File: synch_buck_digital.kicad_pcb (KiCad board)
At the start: 4 copper layers, 60 x 49.6 mm, 48 parts, among them U1 BSC066N06NSATMA1, U2 BSC066N06NSATMA1, U3 INA241A3IDDFR

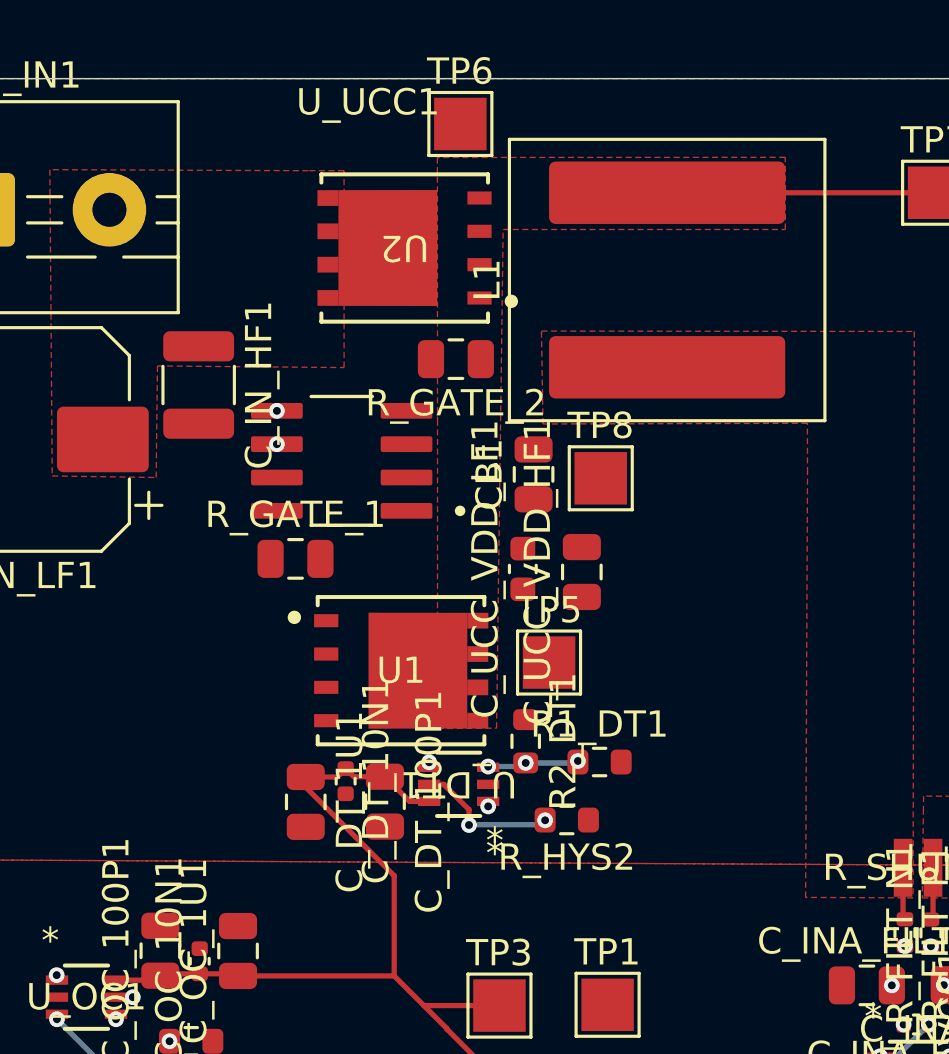
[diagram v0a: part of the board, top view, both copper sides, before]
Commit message: Fixed FET Footprint and updated pour topology
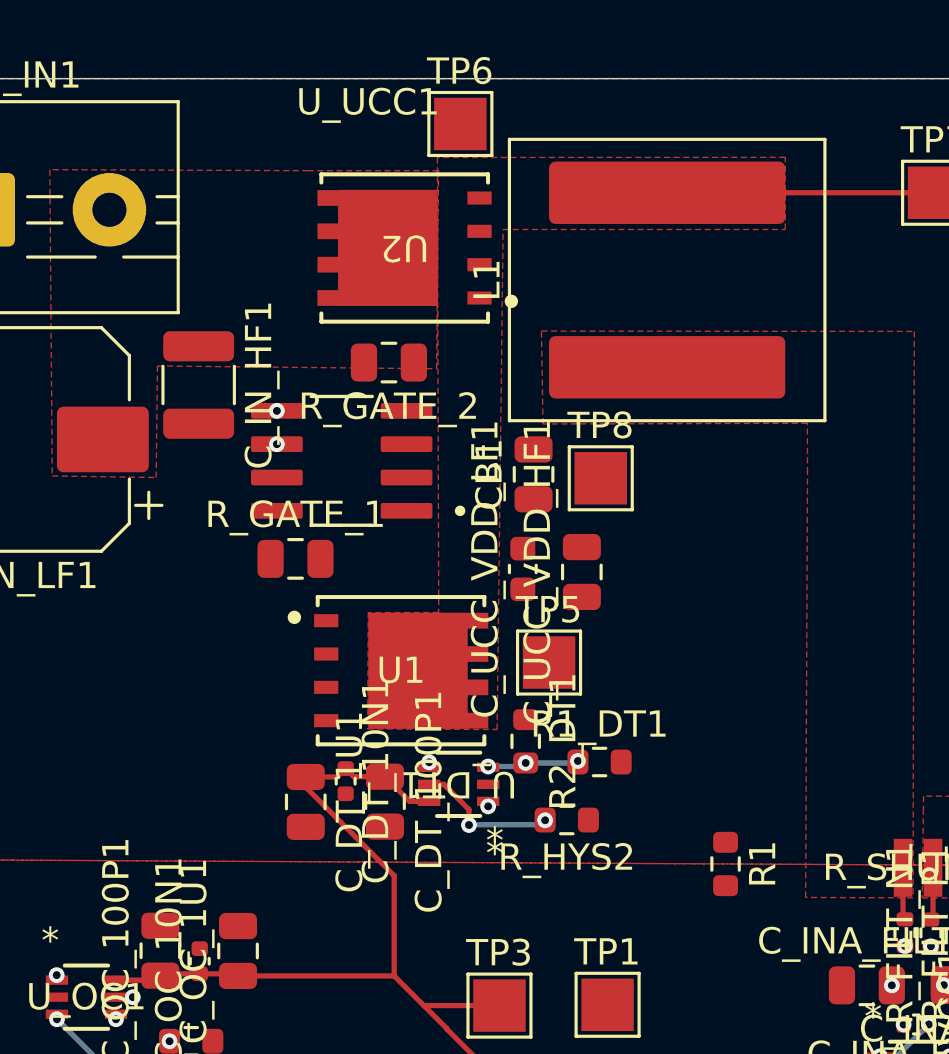
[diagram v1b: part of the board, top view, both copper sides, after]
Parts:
- added R1: 0R, Resistor_SMD:R_0603_1608Metric, F.Cu at (212.5, 83.9)
- moved R_GATE_2 2.55 mm to (199.7, 64.8)
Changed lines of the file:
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@@
 	(footprint "Capacitor_SMD:C_0805_2012Metric"
 		(layer "F.Cu")
-		(at 202.2 64.69 180)
+		(at 199.65 64.82 180)
 		(descr "Capacitor SMD 0805 (2012 Metric), square (rectangular) end terminal, IPC-7351 nominal, (Body size source: IPC-SM-782 page 76, https://www.pcb-3d.com/wordpress/wp-content/uploads/ipc-sm-782a_amendment_1_and_2.pdf, https://docs.google.com/spreadsheets/d/1BsfQQcO9C6DZCsRaXUlFlo91Tg2WpOkGARC1WS5S8t0/edit?usp=sharing)")
 		(tags "capacitor")
@@
 		)
 	)
+	(footprint "Resistor_SMD:R_0603_1608Metric"
+		(layer "F.Cu")
+		(at 212.475 83.925 -90)
+		(descr "Resistor SMD 0603 (1608 Metric), square (rectangular) end terminal, IPC-7351 nominal, (Body size source: IPC-SM-782 page 72, https://www.pcb-3d.com/wordpress/wp-content/uploads/ipc-sm-782a_amendment_1_and_2.pdf)")
+		(tags "resistor")
+		(property "Reference" "R1"
+			(at 0 -1.43 90)
+			(layer "F.SilkS")
+			(effects
+				(font
+					(size 1 1)
+					(thickness 0.15)
+				)
+			)
+		)
+		(property "Value" "0R"
+			(at 0 1.43 90)
+			(layer "F.Fab")
+			(effects
+				(font
+					(size 1 1)
+					(thickness 0.15)
+				)
+			)
+		)
+		(property "Datasheet" ""
+			(at 0 0 90)
+			(layer "F.Fab")
+			(hide yes)
+			(effects
+				(font
+					(size 1.27 1.27)
+				)
+			)
+		)
+		(property "Description" "Resistor, US symbol"
+			(at 0 0 90)
+			(layer "F.Fab")
+			(hide yes)
+			(effects
+				(font
+					(size 1.27 1.27)
+				)
+			)
+		)
+		(property "KiLib_Generator" "SMD_2terminal_chip_molded"
+			(at 0 0 90)
+			(layer "F.SilkS")
+			(hide yes)
+			(effects
+				(font
+					(size 1 1)
+					(thickness 0.15)
+				)
+			)
+		)
+		(property ki_fp_filters "R_*")
+		(sheetname "/")
+		(sheetfile "synch_buck_digital.kicad_sch")
+		(units
+			(unit
+				(name "A")
+				(pins "1" "2")
+			)
+		)
+		(attr smd)
+		(duplicate_pad_numbers_are_jumpers no)
+		(fp_line
+			(start -0.237258 0.5225)
+			(end 0.237258 0.5225)
+			(stroke
+				(width 0.12)
+				(type solid)
+			)
+			(layer "F.SilkS")
+		)
+		(fp_line
+			(start -0.237258 -0.5225)
+			(end 0.237258 -0.5225)
+			(stroke
+				(width 0.12)
+				(type solid)
+			)
+			(layer "F.SilkS")
+		)
+		(fp_rect
+			(start -1.48 -0.73)
+			(end 1.48 0.73)
+			(stroke
+				(width 0.05)
+				(type solid)
+			)
+			(fill no)
+			(layer "F.CrtYd")
+		)
+		(fp_rect
+			(start -0.8 -0.4125)
+			(end 0.8 0.4125)
+			(stroke
+				(width 0.1)
+				(type solid)
+			)
+			(fill no)
+			(layer "F.Fab")
+		)
+		(fp_text user "${REFERENCE}"
+			(at 0 0 90)
+			(layer "F.Fab")
+			(effects
+				(font
+					(size 0.4 0.4)
+					(thickness 0.06)
+				)
+			)
+		)
+		(pad "1" smd roundrect
+			(at -0.825 0 270)
+			(size 0.8 0.95)
+			(layers "F.Cu" "F.Mask" "F.Paste")
+			(roundrect_rratio 0.25)
+			(net "PGND")
+			(pintype "passive")
+		)
+		(pad "2" smd roundrect
+			(at 0.825 0 270)
+			(size 0.8 0.95)
+			(layers "F.Cu" "F.Mask" "F.Paste")
+			(roundrect_rratio 0.25)
+			(net "SGND")
+			(pintype "passive")
+		)
+		(embedded_fonts no)
+		(model "${KICAD10_3DMODEL_DIR}/Resistor_SMD.3dshapes/R_0603_1608Metric.step"
+			(offset
+				(xyz 0 0 0)
+			)
+			(scale
+				(xyz 1 1 1)
+			)
+			(rotate
+				(xyz 0 0 0)
+			)
+		)
+	)
 	(footprint "TestPoint:TestPoint_Pad_2.0x2.0mm"
 		(layer "F.Cu")
@@
 			(unit
 				(name "A")
-				(pins "1" "2" "3" "4" "8" "7" "6" "5")
+				(pins "1" "2" "3" "4" "9" "8" "7" "6" "5")
 			)
 		)
@@
 			)
 			(fill yes)
-			(layer "F.Cu")
-		)
-		(fp_poly
-			(pts
-				(xy 2.525501 -2.204999) (xy -1.240109 -2.2098) (xy -1.240109 2.2098) (xy 2.524502 2.204999) (xy 2.524502 1.605001)
-				(xy 2.524502 0.934999) (xy 2.524502 0.335001) (xy 2.524502 -0.335001) (xy 2.524502 -0.934999) (xy 2.525501 -1.605001)
-			)
-			(stroke
-				(width 0)
-				(type solid)
-			)
-			(fill yes)
 			(layer "F.Mask")
 		)
@@
 			(pintype "unspecified")
 		)
+		(pad "9" smd rect
+			(at -0.21 1.55 180)
+			(size 3.788772 4.425282)
+			(drill
+				(offset 0.856059 -1.546284)
+			)
+			(layers "F.Cu" "F.Mask" "F.Paste")
+			(net "+12V")
+			(pinfunction "EP_9")
+			(pintype "passive")
+		)
 		(embedded_fonts no)
 	)
@@
 			(unit
 				(name "A")
-				(pins "1" "2" "3" "4" "8" "7" "6" "5")
+				(pins "1" "2" "3" "4" "9" "8" "7" "6" "5")
 			)
 		)
@@
 			)
 			(fill yes)
-			(layer "F.Cu")
-		)
-		(fp_poly
-			(pts
-				(xy 2.525501 -2.204999) (xy -1.240109 -2.2098) (xy -1.240109 2.2098) (xy 2.524502 2.204999) (xy 2.524502 1.605001)
-				(xy 2.524502 0.934999) (xy 2.524502 0.335001) (xy 2.524502 -0.335001) (xy 2.524502 -0.934999) (xy 2.525501 -1.605001)
-			)
-			(stroke
-				(width 0)
-				(type solid)
-			)
-			(fill yes)
 			(layer "F.Mask")
 		)
@@
 			(pintype "unspecified")
 		)
+		(pad "9" smd rect
+			(at -0.21 1.55)
+			(size 3.788772 4.425282)
+			(drill
+				(offset 0.856059 -1.546284)
+			)
+			(layers "F.Cu" "F.Mask" "F.Paste")
+			(net "/SW")
+			(pinfunction "EP_9")
+			(pintype "passive")
+		)
 		(embedded_fonts no)
 	)
@@
 		(polygon
 			(pts
-				(xy 214.75 57) (xy 201.495599 57.005836) (xy 201.5 67) (xy 201.5 78.764999) (xy 203.75 78.75) (xy 204 59.75)
-				(xy 214.75 59.75)
+				(xy 214.75 57) (xy 201.495599 57.005836) (xy 201.545634 74.341902) (xy 198.86 74.35) (xy 198.842977 78.780458)
+				(xy 203.770542 78.799391) (xy 204 59.75) (xy 214.75 59.75)
 			)
 		)
@@
 		(polygon
 			(pts
-				(xy 186.73 57.47) (xy 186.82 69.14) (xy 190.78 69.2) (xy 190.83 64.95) (xy 197.94 65.01) (xy 197.94 57.51)
-				(xy 196.58 57.51)
+				(xy 186.73 57.47) (xy 186.82 69.14) (xy 190.78 69.2) (xy 190.83 64.95) (xy 201.464071 65.056988)
+				(xy 201.54 57.51) (xy 196.58 57.51)
 			)
 		)
@@
 		)
 		(min_thickness 0.25)
-		(fill yes
+		(fill
 			(thermal_gap 0.5)
 			(thermal_bridge_width 0.5)

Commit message: pcb finished
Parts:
- moved TP5 14.8 mm to (191.1, 78.3)
- moved C_UCC_VDD_HF1 10.3 mm to (196.7, 72.6), turned to 0 degrees
- moved R_GATE_2 8.72 mm to (202.1, 56.5)
- moved R_GATE_1 5.18 mm to (195.4, 77.4), turned to -90 degrees
- moved C_UCC_VDD_LF1 4.81 mm to (200.0, 72.1), turned to 180 degrees
- moved CB1 3.78 mm to (204.9, 72.8), turned to -90 degrees
- moved TP8 3.78 mm to (207.5, 73.0)
- moved TP6 3.72 mm to (206.0, 56.5)
- moved TP7 3.53 mm to (218.2, 61.0)
- moved L1 2.55 mm to (210.1, 64.2)
- moved C_INA_VCC1 0.61 mm to (222.7, 92.0)
- moved R1 0.16 mm to (212.5, 83.8)
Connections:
- C_DT_100P1 pad 2: SGND -> PGND
- C_DT_10N1 pad 2: SGND -> PGND
- C_DT_1U1 pad 2: SGND -> PGND
- U_UCC1 pad 7: SGND -> PGND
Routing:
- net Net-(U_UCC1-HO): track 0.00 -> 18.0 mm, vias 0 -> 2
- net +12V: track 0.00 -> 12.8 mm
- net /BOOT: track 0.00 -> 8.76 mm, vias 0 -> 3
- net /GATE_LS: track 0.00 -> 6.24 mm
- net Net-(U_UCC1-LO): track 0.00 -> 6.22 mm, vias 0 -> 2
- net /GATE_HS: track 0.00 -> 5.16 mm
- net SGND: track 0.00 -> 5.10 mm
- net /SW: track 10.2 -> 14.2 mm
- net +5V: track 58.6 -> 60.6 mm
- net PGND: track 0.00 -> 1.17 mm

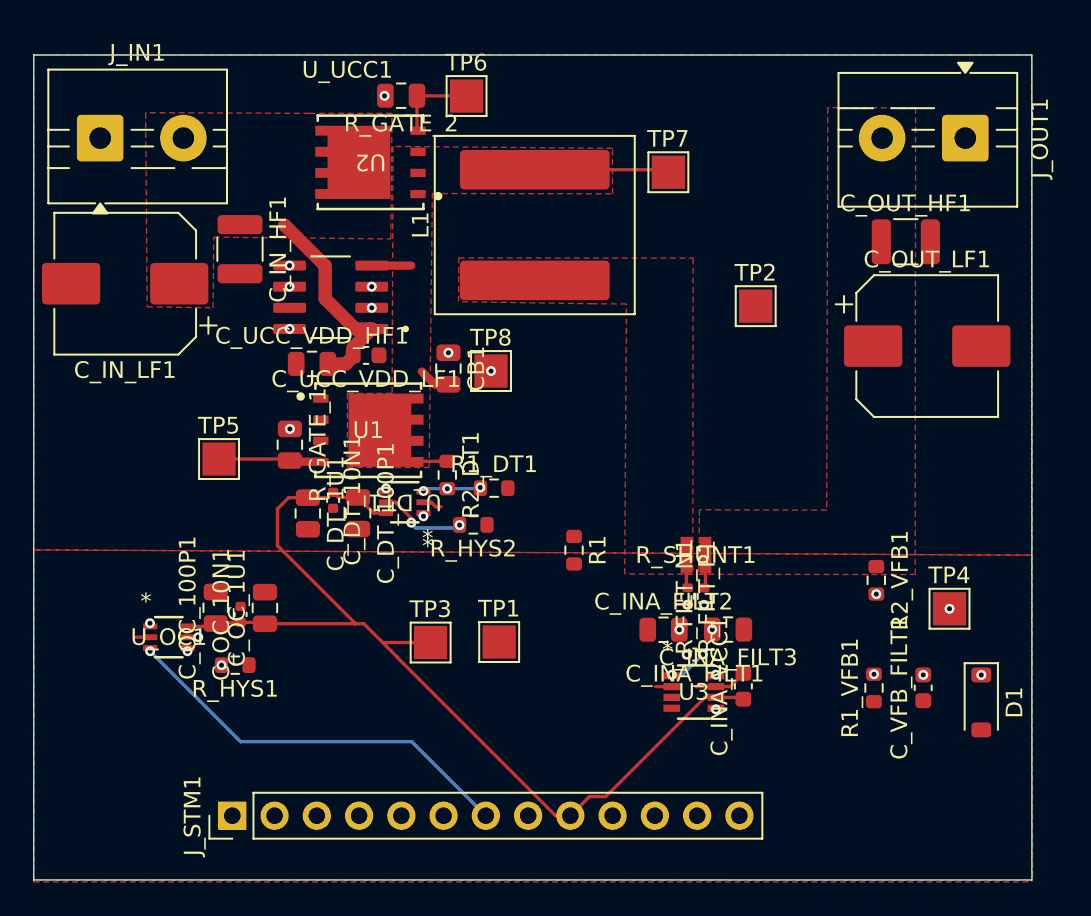
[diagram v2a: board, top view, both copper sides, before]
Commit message: Reduced board size
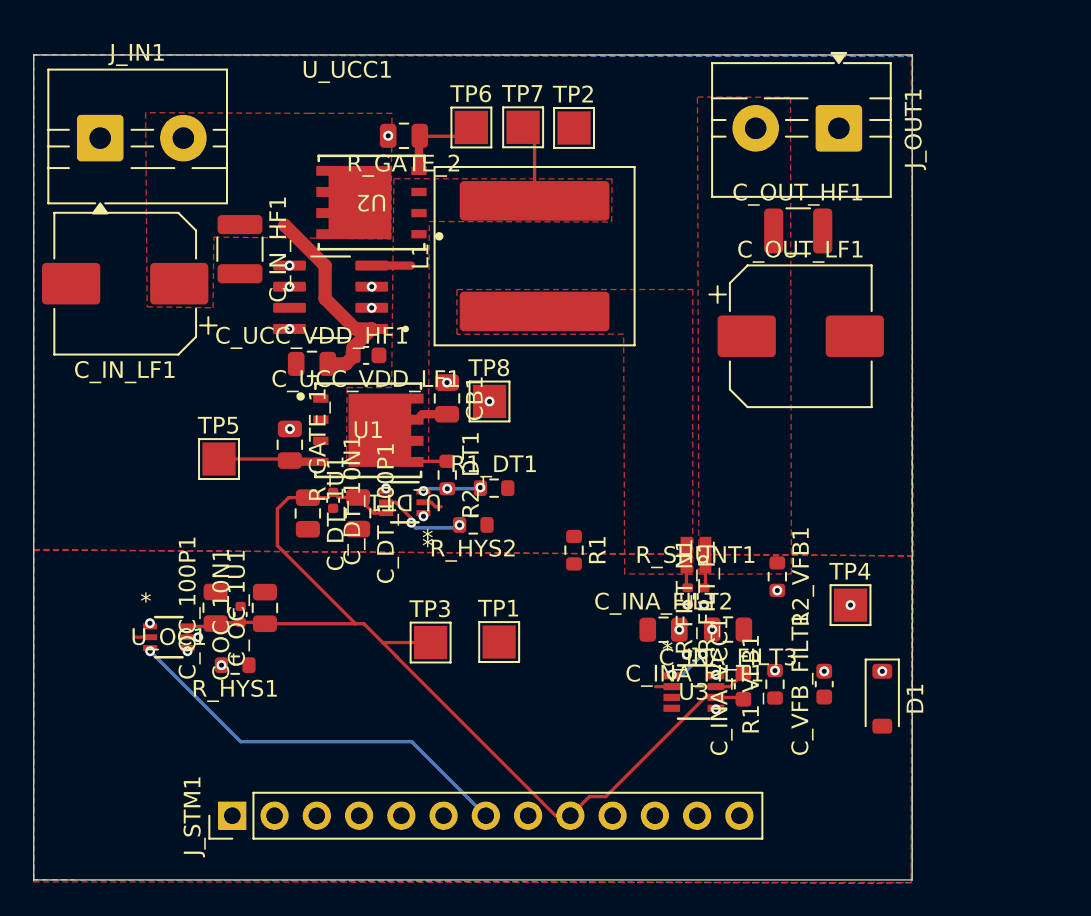
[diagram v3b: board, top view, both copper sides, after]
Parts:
- moved TP2 15.3 mm to (212.5, 58.4)
- moved TP7 9.14 mm to (209.4, 58.4)
- moved C_OUT_LF1 7.62 mm to (226.1, 70.9)
- moved J_OUT1 7.62 mm to (228.4, 58.4)
- moved C_OUT_HF1 6.50 mm to (226.0, 64.6)
- moved TP4 5.95 mm to (229.1, 87.1)
- moved D1 5.95 mm to (231.0, 92.7)
- moved R2_VFB1 5.95 mm to (224.7, 85.4)
- moved C_VFB_FILT1 5.95 mm to (227.5, 91.8)
- moved R1_VFB1 5.95 mm to (224.6, 91.8)
- moved R_GATE_2 2.42 mm to (202.3, 58.9)
- moved U2 2.42 mm to (200.3, 62.9)
- moved TP6 1.91 mm to (206.3, 58.4)
- moved L1 1.87 mm to (210.1, 66.1)
- moved TP8 1.83 mm to (207.4, 74.8)
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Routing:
- net /SW: track 14.2 -> 10.9 mm
- net Net-(U_UCC1-HO): track 18.0 -> 15.8 mm
- net /BOOT: track 8.76 -> 10.6 mm
- net /GATE_HS: track 5.16 -> 5.98 mm
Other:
- board size 60 x 49.6 mm -> 52.8 x 49.6 mm
